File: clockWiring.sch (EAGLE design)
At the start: 11 parts

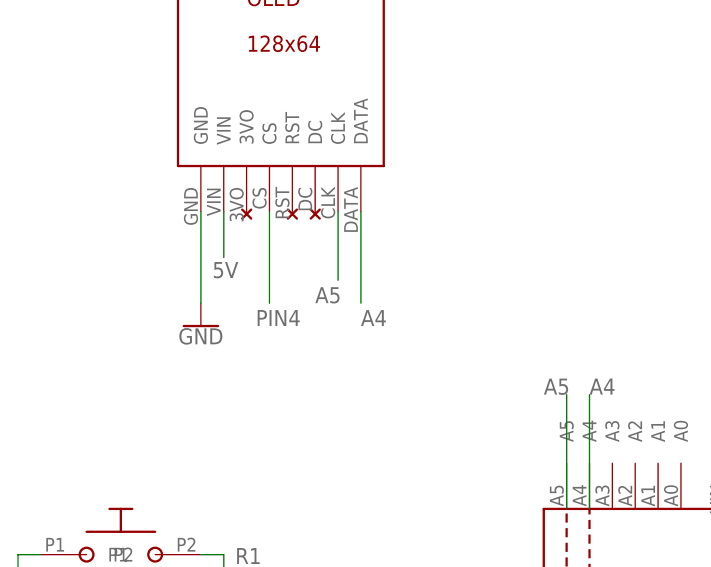
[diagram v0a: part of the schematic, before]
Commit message: fix missasignment of pin4
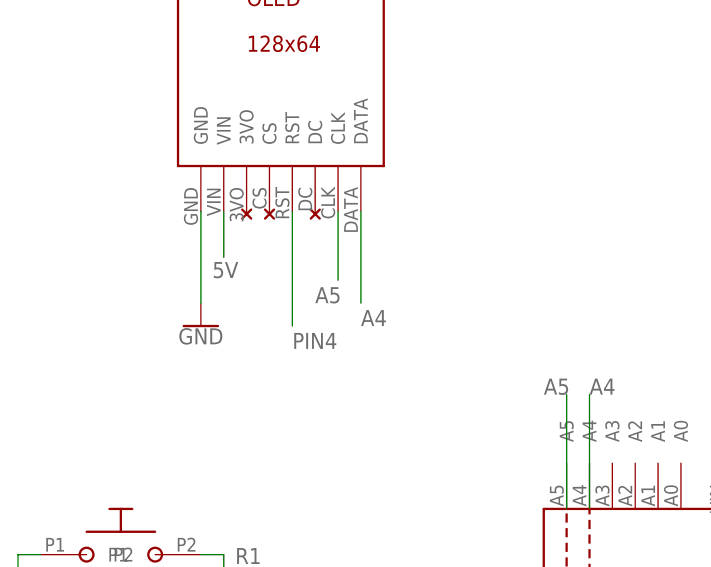
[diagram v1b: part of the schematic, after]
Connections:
- net PIN4: now also U$2.RST; no longer U$2.CS
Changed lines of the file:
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@@
 </instance>
 <instance part="U$3" gate="G$1" x="91.948" y="136.398" smashed="yes"/>
-<instance part="U$4" gate="G$1" x="97.028" y="136.398" smashed="yes"/>
+<instance part="U$4" gate="G$1" x="94.488" y="136.398" smashed="yes"/>
 <instance part="U$5" gate="G$1" x="180.34" y="129.54" smashed="yes"/>
 <instance part="SP1" gate="S1" x="248.92" y="149.86" smashed="yes">
@@
 <net name="PIN4" class="0">
 <segment>
-<pinref part="U$2" gate="G$1" pin="CS"/>
-<wire x1="93.98" y1="137.16" x2="93.98" y2="127" width="0.1524" layer="91"/>
-<label x="92.456" y="124.46" size="1.778" layer="95"/>
-</segment>
-<segment>
 <pinref part="U$6" gate="G$1" pin="4"/>
 <wire x1="137.16" y1="76.2" x2="137.16" y2="63.5" width="0.1524" layer="91"/>
 <label x="134.62" y="60.96" size="1.778" layer="95"/>
 </segment>
+<segment>
+<pinref part="U$2" gate="G$1" pin="RST"/>
+<wire x1="96.52" y1="137.16" x2="96.52" y2="124.46" width="0.1524" layer="91"/>
+<label x="96.52" y="121.92" size="1.778" layer="95"/>
+</segment>
 </net>
